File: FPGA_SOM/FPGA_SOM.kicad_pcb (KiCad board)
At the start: 6 copper layers, 30.5 x 47 mm, 88 parts, among them J1 Conn_01x02, J2 USB_C_Receptacle_USB2.0, J3 Conn_02x06_Top_Bottom, J4 Conn_02x04_Counter_Clockwise, J5 Conn_01x06, J6 Conn_01x06, SW1 SW_Push, SW2 SW_Push, SW3 SW_Push, U1 W25Q128JVSIQ, U2 ICE40UP5K-SG48ITR, U3 AP2127N-3.3, U4 AP2127N-1.2, X1 SX2M36.000B10F20TNN

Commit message: Final version 3 sent for assembly.
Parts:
- J3: footprint Connector_PinHeader_2.54mm:PinHeader_2x06_P2.54mm_Horizontal -> Connector_PinSocket_2.54mm:PinSocket_2x06_P2.54mm_Horizontal
- J5, J6: footprint Connector_PinHeader_2.54mm:PinHeader_1x06_P2.54mm_Horizontal -> Connector_PinSocket_2.54mm:PinSocket_1x06_P2.54mm_Horizontal
- moved J5 12.7 mm to (126.7, 36.8), turned to 0 degrees
- moved J6 12.7 mm to (154.6, 49.5), turned to 180 degrees
- moved J3 12.7 mm to (147.0, 26.6), turned to -90 degrees

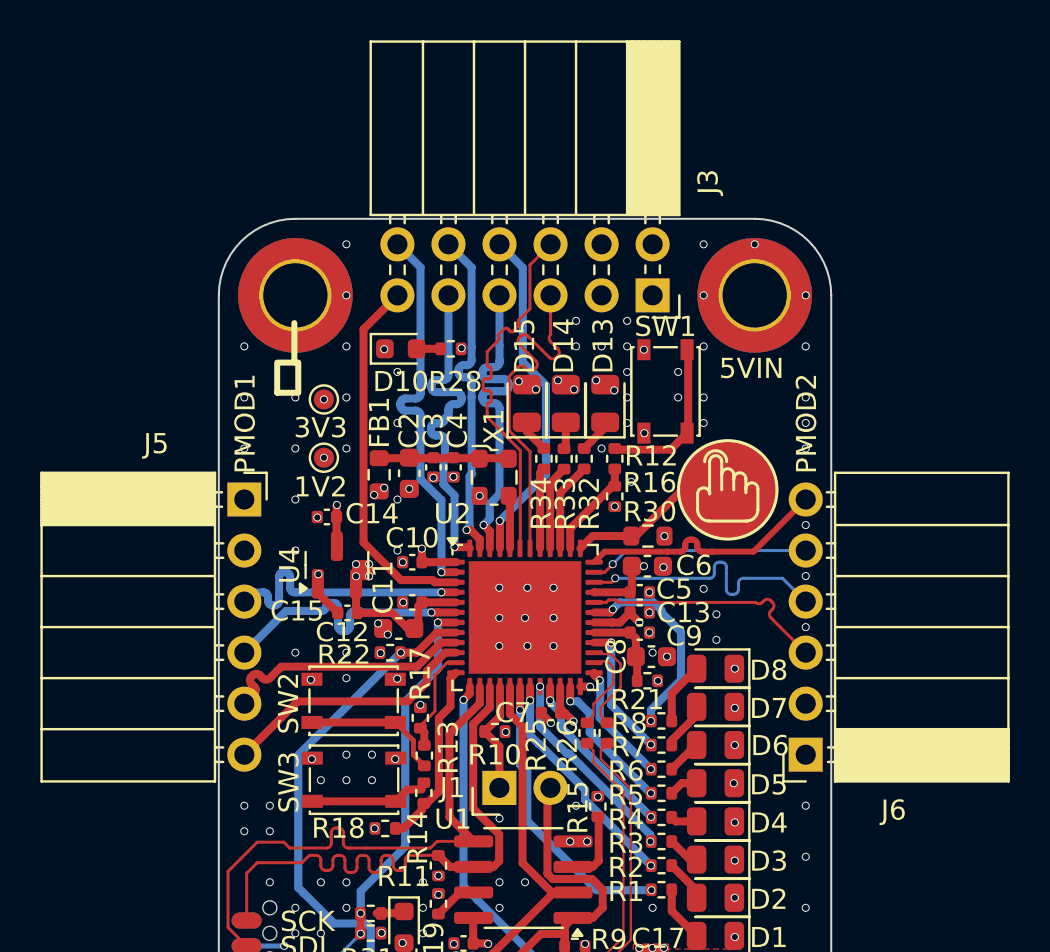
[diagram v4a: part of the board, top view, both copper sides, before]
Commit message: Kicad Update changes some things. Also reorganise nets.
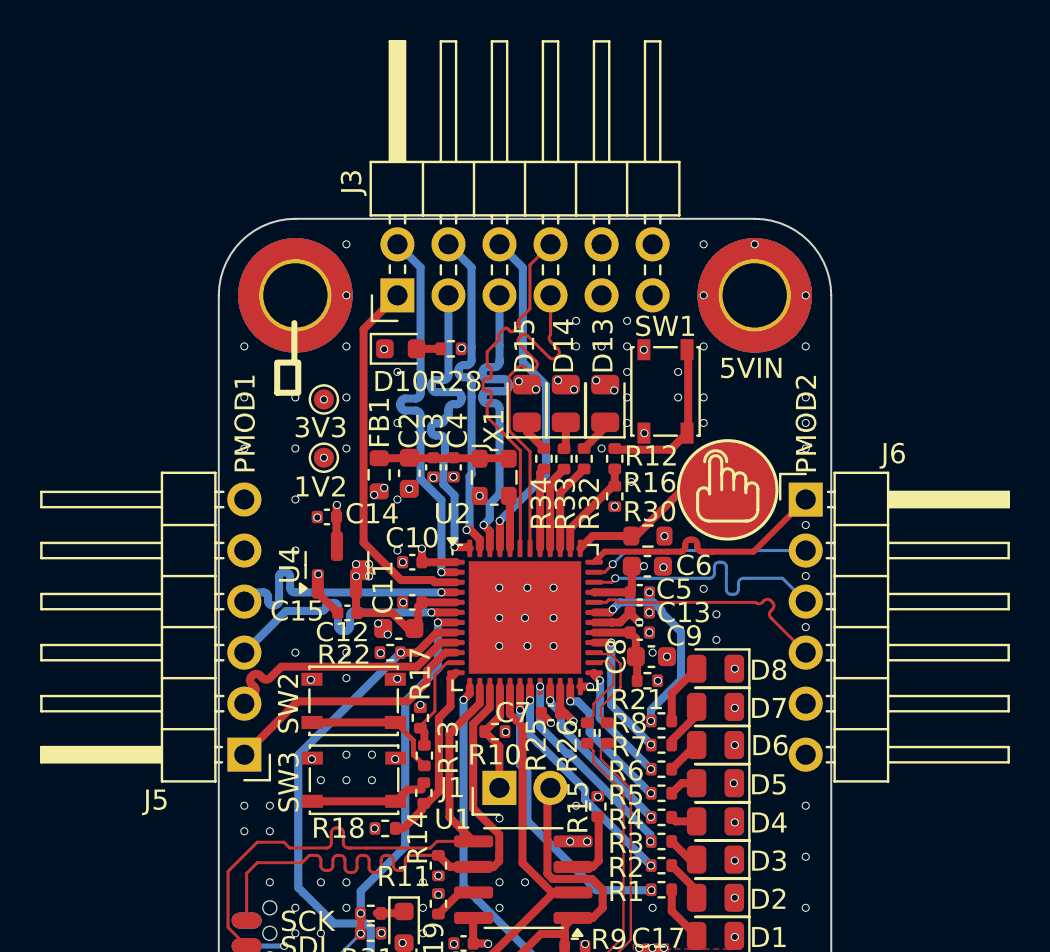
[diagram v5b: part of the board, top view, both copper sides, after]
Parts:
- J3: footprint Connector_PinSocket_2.54mm:PinSocket_2x06_P2.54mm_Horizontal -> Connector_PinHeader_2.54mm:PinHeader_2x06_P2.54mm_Horizontal
- J5, J6: footprint Connector_PinSocket_2.54mm:PinSocket_1x06_P2.54mm_Horizontal -> Connector_PinHeader_2.54mm:PinHeader_1x06_P2.54mm_Horizontal
- R25, R26: value 68 -> 22
- moved J5 12.7 mm to (126.7, 49.5), turned to 180 degrees
- moved J6 12.7 mm to (154.6, 36.8), turned to 0 degrees
- moved J3 12.7 mm to (134.3, 26.6), turned to 90 degrees
